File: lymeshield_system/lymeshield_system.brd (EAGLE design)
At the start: 67.9 x 49.5 mm, 67 parts, among them J1 TSW-106-07-G-S, J2 TSW-103-07-G-D-LL, J3 M04B, J4 1844210, U1 ATMEGA1608-MU, U10 MCP79410-I_SN, U12 STSPIN240, U2 MX25V1635FM1I, U3 STLQ015M33R, U4 DRV5057A2QDBZ, U5 OPA2349EA, Y1 ECS-.327-9-1210-TR, Y2 ECS-.327-9-1210-TR

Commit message: refactor: fixed ignored files and added tables
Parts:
- removed U10: MCP79410-I_SN, HatchPoint-MicrochipTechnology:SOIC127P600X175-8N
- removed U12: STSPIN240, HatchPoint-TI:VFQFPN(3X3X1.0MM-16L)
- added U6: DRV5057A2QDBZ, HatchPoint-TI:SOT95P237X112-3N
- added U7: STLQ015M33R, HatchPoint-ST:SOT23-5L
- C11: value 10nF -> 100nF
- C12: value 1000pF -> 22uF; device HatchPoint-Capacitors:CAPC_0603_1608X90N -> HatchPoint-Capacitors:CAPC_1206
- C13: value 10nF -> 2.2uF; device HatchPoint-Capacitors:CAPC_0603_1608X90N -> HatchPoint-Capacitors:CAPC_1206
- C14: value 22nF -> 10nF
- C15: value 1.00uF -> 10nF
- C16: value 1.00uF -> 100nF
- C17: value 22uF -> 1000pF; device HatchPoint-Capacitors:CAPC_1206 -> HatchPoint-Capacitors:CAPC_0603_1608X90N
- C18: value 2.2uF -> 22nF; device HatchPoint-Capacitors:CAPC_1206 -> HatchPoint-Capacitors:CAPC_0603_1608X90N
- C2: value 15.0pF -> 100nF; device HatchPoint-Capacitors:CAPC_0402_1005X55N -> HatchPoint-Capacitors:CAPC_0603_1608X90N
- C20, C21, C4: value 100nF -> 1.00uF
- C3: value 15.0pF -> 1.00uF; device HatchPoint-Capacitors:CAPC_0402_1005X55N -> HatchPoint-Capacitors:CAPC_0603_1608X90N
- C5, C6: value 1.00uF -> 15.0pF; device HatchPoint-Capacitors:CAPC_0603_1608X90N -> HatchPoint-Capacitors:CAPC_0402_1005X55N
- J2: value TSW-103-07-G-D-LL -> M04B; device HatchPoint-Samtec:HDRV6W64P254_2X3_762X495X838P -> HatchPoint-JST:SM04B-SRSS-TB(LFSN)
- J3: value M04B -> TSW-103-07-G-D-LL; device HatchPoint-JST:SM04B-SRSS-TB(LFSN) -> HatchPoint-Samtec:HDRV6W64P254_2X3_762X495X838P
- R1, R3: value 1.00K -> 4.70K
- R11: value 1.00K -> 620mOhm; device HatchPoint-Resistors:R0603K -> HatchPoint-Resistors:R0805K
- R12: value 47.0K -> 620mOhm; device HatchPoint-Resistors:R0603K -> HatchPoint-Resistors:R0805K
- R13: value 620mOhm -> 18.0K; device HatchPoint-Resistors:R0805K -> HatchPoint-Resistors:R0603K
- R14: value 620mOhm -> 1.00K; device HatchPoint-Resistors:R0805K -> HatchPoint-Resistors:R0603K
- R15: value 1.00K -> 47.0K
- R16, R17, R18: value 1.20M -> 1.00K
- R19, R20: value 1.00K -> 1.20M
- R4, R5: value 4.70K -> 1.00K
- R7, R8: value 18.0K -> 1.20M
- R9: value 1.20M -> 18.0K
- U1: value ATMEGA1608-MU -> MCP79410-I_SN; device HatchPoint-MicrochipTechnology:QFN50P500X500X90-33N -> HatchPoint-MicrochipTechnology:SOIC127P600X175-8N
- U2: value MX25V1635FM1I -> ATMEGA1608-MU; device HatchPoint-Macronix:SOIC127P600X175-8N -> HatchPoint-MicrochipTechnology:QFN50P500X500X90-33N
- U3: value STLQ015M33R -> MX25V1635FM1I; device HatchPoint-ST:SOT23-5L -> HatchPoint-Macronix:SOIC127P600X175-8N
- U4: value DRV5057A2QDBZ -> OPA2349EA; device HatchPoint-TI:SOT95P237X112-3N -> HatchPoint-OPAMPs:SOT65P280X145-8N
- U5: value OPA2349EA -> STSPIN240; device HatchPoint-OPAMPs:SOT65P280X145-8N -> HatchPoint-TI:VFQFPN(3X3X1.0MM-16L)
- moved R20 46.4 mm to (10.8, 12.1), turned to 180 degrees
- moved J2 46.3 mm to (19.1, 36.5), flipped to the top, turned to 180 degrees
- moved J3 46.3 mm to (60.6, 16.2), flipped to the bottom, turned to 270 degrees
- moved Q1 43.5 mm to (50.2, -5.08), turned to 0 degrees
- moved R1 42.1 mm to (21.6, 25.7), turned to 270 degrees
- moved R4 42.1 mm to (57.1, 3.17), turned to 0 degrees
- moved R5 41.6 mm to (57.1, 6.99), turned to 0 degrees
- moved Q3 41.1 mm to (11.7, 9.53), turned to 90 degrees
- moved C21 39.8 mm to (17.8, 11.1)
- moved R17 39.4 mm to (51.8, -9.84)
- moved R9 37.6 mm to (48.3, 15.7), turned to 270 degrees
- moved R16 36.6 mm to (47.3, -7.94)
- moved C16 34.3 mm to (47.3, -6.35), turned to 90 degrees
- moved C15 33.3 mm to (45.1, 14.3), turned to 90 degrees
- moved Q2 33.1 mm to (33.0, 34.9), turned to 270 degrees
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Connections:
- net !CS_FLASH: now also U3.1; no longer U1.1
- net !GRN_LED_EN: now also U2.11; no longer U1.11
- net !MTR_FAULT: now also J3.4, U2.15; no longer J2.4, U1.15
- net !MTR_STBY: now also C17.1, R13.2, U2.17, U5.14; no longer C12.1, R7.2, U1.17, U12.14
- net !RED_LED_EN: now also U2.10; no longer U1.10
- net !RST: now also C7.1, R3.2, U2.26; no longer C1.1, R2.2, U1.26
- net AN0_BAT_LVL: now also U2.13, U4.1, U4.2; no longer U1.13, U5.1, U5.2
- net AN1_HALL_FILT: now also U2.14, U4.6, U4.7; no longer U1.14, U5.6, U5.7
- net AVDD: now also C4.1, U2.18; no longer C6.1, U1.18
- net BKUP_BATTERY: now also Q2.1, U1.3; no longer Q1.1, U10.3
- net DGND: now also C11.1, C20.2, C21.2, J2.1, J2.5, Q1.2, Q2.3, R10.2, R11.2, R15.2, R19.2, R20.2, U1.4, U2.19, U2.29, U2.33, U3.4, U4.4, U5.17, U5.7, U7.2; no longer C11.2, C16.2, C20.1, J3.1, J3.5, Q1.3, Q3.2, R13.2, R14.2, R17.2, R18.2, R9.2, U1.19, U1.29, U1.33, U10.4, U12.17, U12.7, U2.4, U3.2, U5.4
- net GPIO_PC1: now also U2.7; no longer U1.7
- net HALL_PWM_SENSE: now also J3.5, R16.2, R17.1, U2.24, U6.2; no longer J2.5, R19.2, R20.1, U1.24, U4.2
- net HALL_PWR_EN: now also R18.1, U2.16; no longer R15.1, U1.16
- net I2C0_SCL: now also J2.4, R2.2, U1.6, U2.9; no longer J3.4, R5.2, U1.9, U10.6
- net I2C0_SDA: now also J2.3, R1.2, U1.5, U2.8; no longer J3.3, R4.2, U1.8, U10.5
- net MTR_CUR_LIMIT: now also J3.2, R9.1, U2.12; no longer J2.2, R6.1, U1.12
- net MTR_EN: now also R6.1, U2.22; no longer R10.1, U1.22
- net MTR_FAULT: now also C14.1, R6.2, U5.13; no longer C13.1, R10.2, U12.13
- net MTR_PHA: now also J3.1, U2.23, U5.1; no longer J2.1, U1.23, U12.1
- net MTR_PHB: now also U5.15; no longer U12.15
- net MTR_PWMA: now also J3.3, U2.25, U5.2; no longer J2.3, U1.25, U12.2
- net MTR_PWMB: now also U5.16; no longer U12.16
- net N$1: now also C8.1, U2.20, Y2.1; no longer C2.1, U1.20, Y1.1
- net N$10: now also R7.2, R8.1, U4.3; no longer R16.2, R17.1, U5.3
- net N$11: now also C18.1, R14.2; no longer C14.1, R11.2
- net N$14: now also Q3.2; no longer Q2.2
- net N$16: now also C9.1, U2.21, Y2.2; no longer C3.1, U1.21, Y1.2
- net N$17: now also C6.1, U1.1, Y1.2; no longer C9.1, U10.1, Y2.2
- net N$19: now also C15.1, R10.1, R9.2, U5.11; no longer C11.1, R6.2, R8.1, U12.11
- net N$2: now also C5.1, U1.2, Y1.1; no longer C8.1, U10.2, Y2.1
- net N$20: now also C19.1, R17.2, U4.5; no longer C21.1, R20.2, U5.5
- net N$23: now also C16.2, Q1.1, U6.3; no longer C21.2, Q3.1, U4.3
- net N$3: now also R14.1, R15.1, U5.12; no longer R11.1, R12.1, U12.12
- net N$5: now also Q1.3, R18.2, R19.1; no longer Q3.3, R15.2, R18.1
- net N$6: now also Q3.3, R20.1; no longer Q2.3, R9.1
- net N$7: now also Q2.2; no longer Q1.2
- net N$8: now also R4.2; no longer R1.2
- net N$9: now also R5.2; no longer R3.2
- net OUTA1: now also U5.3; no longer U12.3
- net OUTA2: now also U5.5; no longer U12.5
- net RTCC_ALARM_INT: now also U1.7, U2.32; no longer U1.32, U10.7
- net SENSEA: now also R11.1, R12.1, U5.4; no longer R13.1, R14.1, U12.4
- net SPI0_MISO: now also U2.3, U3.2; no longer U1.3, U2.2
- net SPI0_MOSI: now also U2.2, U3.5; no longer U1.2, U2.5
- net SPI0_SCK: now also U2.4, U3.6; no longer U1.4, U2.6
- net UART_RX: now also U2.31; no longer U1.31
- net UART_TX: now also U2.30; no longer U1.30
- net UPDI: now also U2.27; no longer U1.27
- net VCC: now also C1.1, C11.2, C2.1, C21.1, C3.1, J2.2, R13.1, R16.1, U1.8, U2.28, U3.8, U4.8, U6.1, U7.5; no longer C19.1, C20.2, C4.1, C5.1, C7.1, J3.2, R19.1, R7.1, U1.28, U10.8, U2.8, U3.5, U4.1, U5.8
- net V_BAT: now also C12.1, C13.1, C20.1, Q3.1, R7.1, U5.6, U7.1, U7.3; no longer C15.1, C17.1, C18.1, Q2.1, R16.1, U12.6, U3.1, U3.3

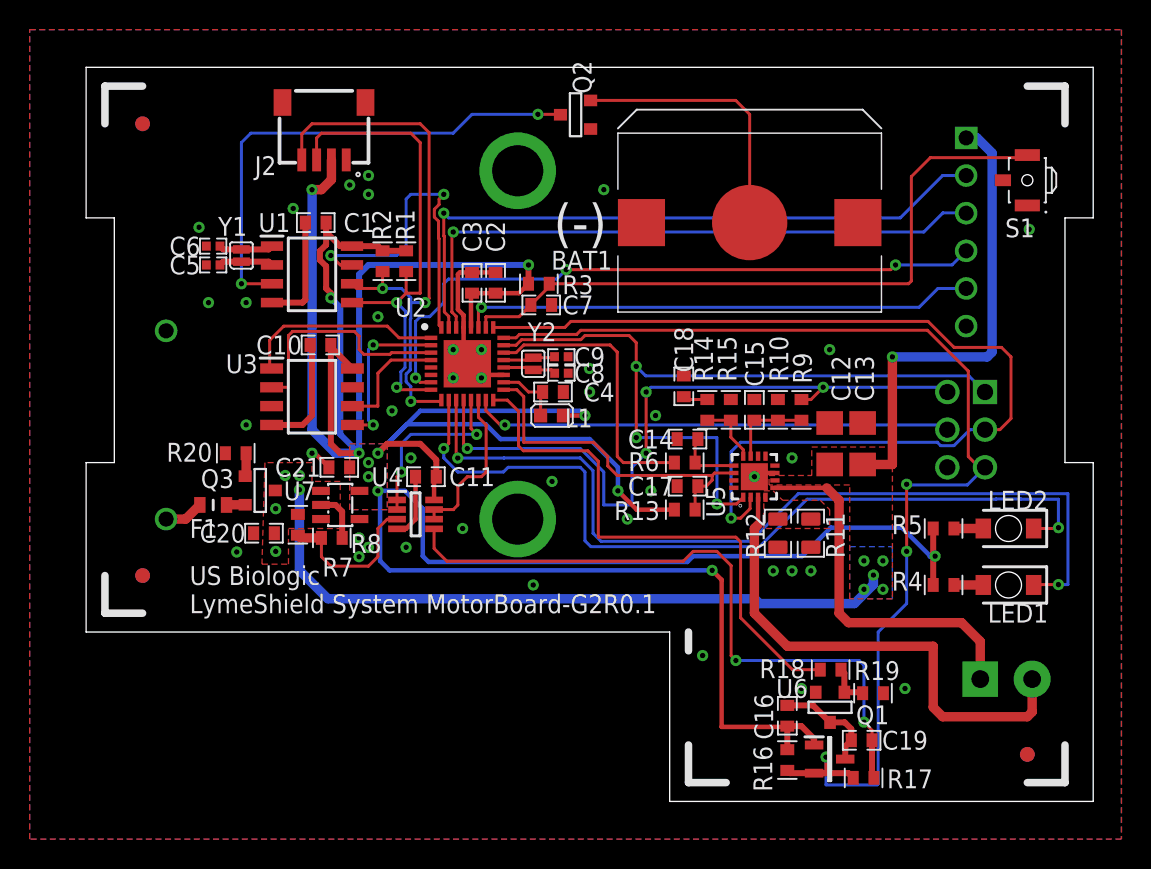
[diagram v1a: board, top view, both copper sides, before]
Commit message: feat: partial changes for r1,1 - Moved cur_limit to TBC0 pin - Modify layout to reduce EMI - Change programming header to match PICKit4 - Merge mtr_cur_limit into !mtr_cur_limit net
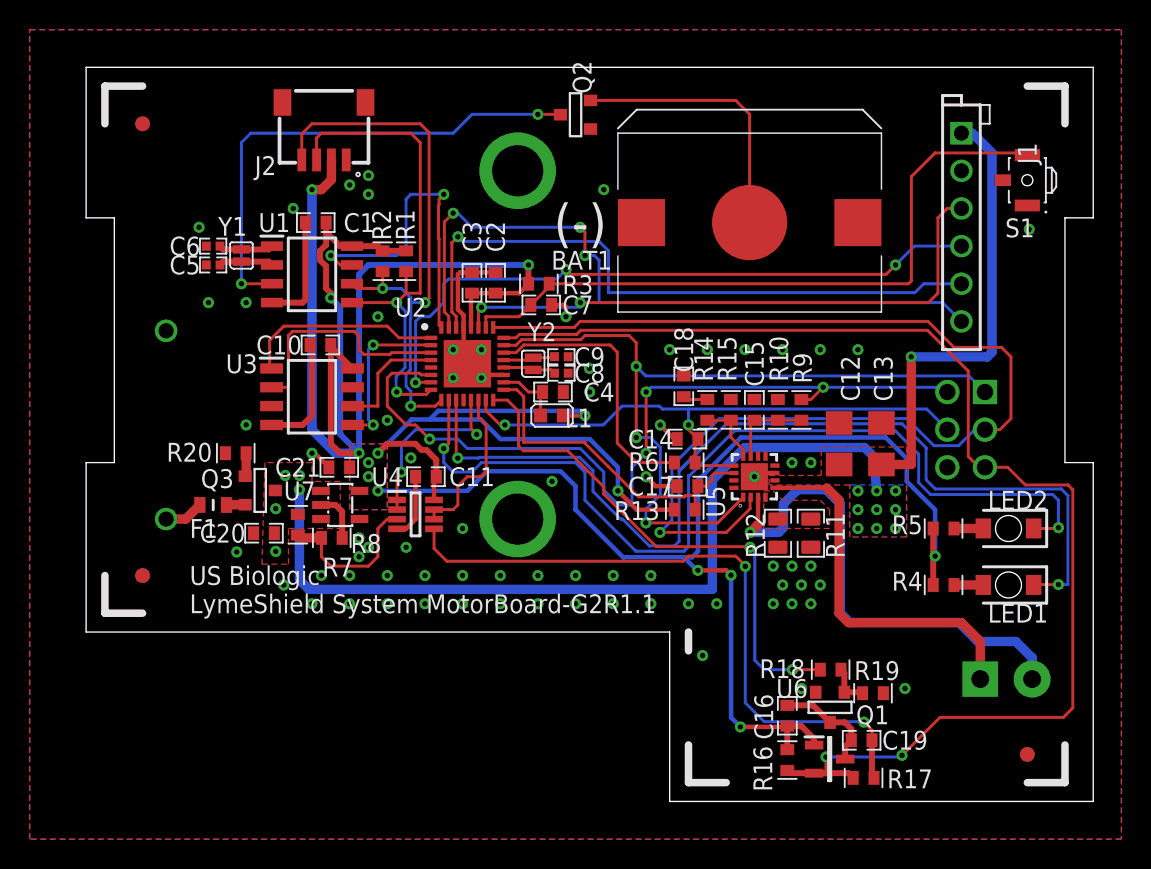
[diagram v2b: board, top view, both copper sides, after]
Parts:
- J1: value TSW-106-07-G-S -> TSW-106-16-L-S-RA; device HatchPoint-Samtec:HDR-100MIL-1X6-THRU -> HatchPoint-Samtec:HDR-100MIL-1X6-THRU-RA
- moved C13 1.27 mm to (53.7, 12.7)
- moved C12 0.63 mm to (50.8, 12.7)
- moved J1 0.45 mm to (59.1, 33.7), flipped to the top
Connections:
- removed net MTR_FAULT: C14.1, R6.2, U5.13
- net !MTR_FAULT: now also C14.1, R6.2, U5.13
- net DGND: now also J1.2; no longer J1.6
- net MTR_CUR_LIMIT: now also U2.6; no longer U2.12
- net UART_RX: now also J1.6; no longer J1.3
- net UART_TX: now also J1.5; no longer J1.2
- net UPDI: now also J1.3; no longer J1.5
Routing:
- net VCC: track 230.5 -> 211.6 mm, vias 12 -> 14
- net MTR_PWMA: track 67.1 -> 78.3 mm
- net V_BAT: track 78.0 -> 86.8 mm, vias 11 -> 15
- net !GRN_LED_EN: track 59.7 -> 68.5 mm
- net !MTR_FAULT: track 32.4 -> 40.1 mm, vias 1 -> 2
- net MTR_CUR_LIMIT: track 47.8 -> 55.4 mm
- net HALL_PWM_SENSE: track 78.7 -> 85.7 mm, vias 3 -> 2
- net !RED_LED_EN: track 55.9 -> 62.7 mm
- net DGND: track 36.6 -> 42.2 mm, vias 40 -> 74
- net UPDI: track 34.7 -> 39.8 mm, vias 1 -> 2
- net MTR_FAULT: track 4.36 -> 0.00 mm
- net UART_RX: track 44.4 -> 48.0 mm, vias 1 -> 3
- net MTR_PHA: track 52.0 -> 54.8 mm
- net UART_TX: track 41.7 -> 43.8 mm
- net HALL_PWR_EN: track 37.0 -> 35.6 mm, vias 0 -> 2
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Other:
- board text added: "US Biologic LymeShield System MotorBoard-G2R1.1"
- board text added: "VCC GND PDG GPIO TXD RXD"
- board text removed: "US Biologic LymeShield System MotorBoard-G2R0.1"
- board text removed: "VCC TXD RXD GPIO OPDI GND"

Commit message: fix: updates for R2.1 board - Change layout for high current routes - Correct routing errors (mtr_cur_limit) - Change tantalum cap to 1210 and give more space
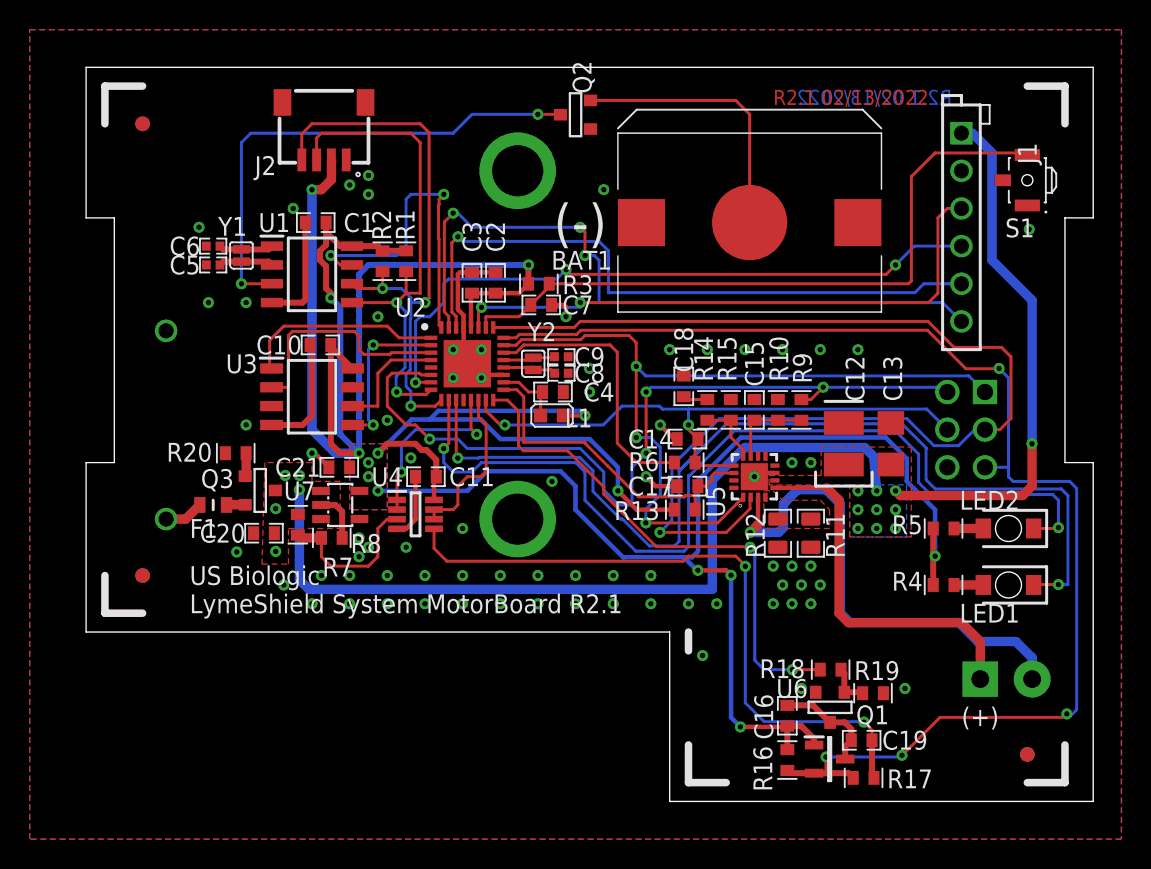
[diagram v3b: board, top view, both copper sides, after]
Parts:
- C12: value 22uF -> TAJB226M010RNJ; device HatchPoint-Capacitors:CAPC_1206 -> HatchPoint-Capacitors:PCAPC_1210
- moved C13 0.63 mm to (54.3, 12.7)
- moved C12 0.32 mm to (51.1, 12.7)
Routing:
- net V_BAT: track 86.8 -> 91.8 mm
- net HALL_PWM_SENSE: track 85.7 -> 88.7 mm, vias 2 -> 4
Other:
- board text added: "(+)"
- board text added: "R2.1 02/13/2022"
- board text added: "US Biologic LymeShield System MotorBoard R2.1"
- board text removed: "US Biologic LymeShield System MotorBoard Gen2 R0.1"
- board text removed: "US Biologic LymeShield System MotorBoard-G2R1.1"

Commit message: fix(lss):  update to R2.2 - Change motor driver
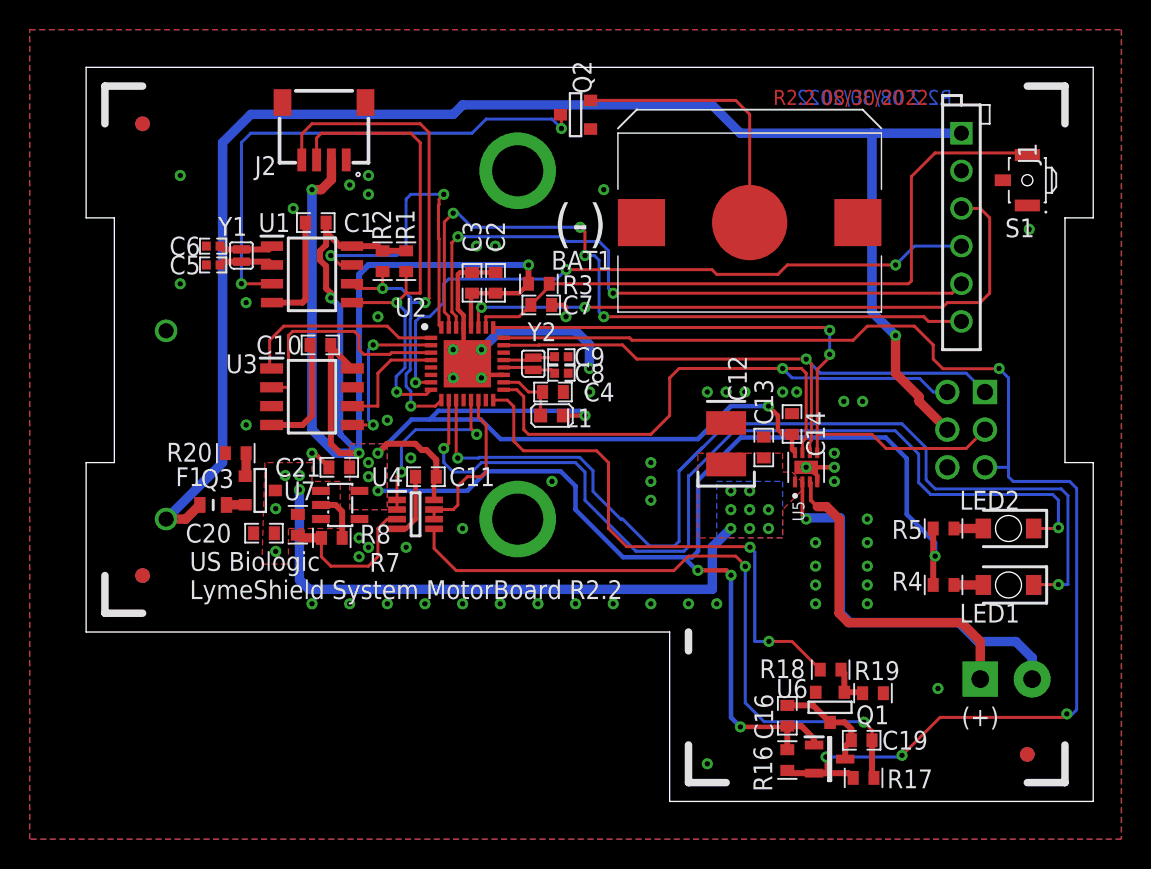
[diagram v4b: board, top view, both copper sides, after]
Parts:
- removed C15: 10nF, HatchPoint-Capacitors:CAPC_0603_1608X90N
- removed C17: 1000pF, HatchPoint-Capacitors:CAPC_0603_1608X90N
- removed C18: 22nF, HatchPoint-Capacitors:CAPC_0603_1608X90N
- removed R10, R13, R6, R9: 18.0K, HatchPoint-Resistors:R0603K
- removed R11, R12: 620mOhm, HatchPoint-Resistors:R0805K
- removed R14: 1.00K, HatchPoint-Resistors:R0603K
- removed R15: 47.0K, HatchPoint-Resistors:R0603K
- C13: value 2.2uF -> 100nF; device HatchPoint-Capacitors:CAPC_1206 -> HatchPoint-Capacitors:CAPC_0603_1608X90N
- C14: value 10nF -> 100nF
- U5: value STSPIN240 -> DRV8838DSGR; device HatchPoint-TI:VFQFPN(3X3X1.0MM-16L) -> HatchPoint-MotionControl:SON50P200X200X80-9N
- moved C13 8.63 mm to (45.7, 11.7)
- moved C12 7.94 mm to (43.2, 12.7)
- moved C14 6.36 mm to (47.6, 13.3), turned to 90 degrees
- moved U5 3.55 mm to (48.6, 11.1)
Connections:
- removed net !MTR_FAULT: C14.1, J3.4, R6.2, U2.15, U5.13
- removed net MTR_CUR_LIMIT: J3.2, R9.1, U2.6
- removed net MTR_EN: R6.1, U2.22
- removed net MTR_PHB: U5.15
- removed net MTR_PWMB: U5.16
- removed net N$11: C18.1, R14.2
- removed net N$15: BAT2.1, F1.1
- removed net N$19: C15.1, R10.1, R9.2, U5.11
- removed net N$3: R14.1, R15.1, U5.12
- removed net SENSEA: R11.1, R12.1, U5.4
- new net V_BAT_IN: BAT2.1, F1.1, J1.1, J3.4
- net !MTR_STBY: now also J3.2, U5.7; no longer C17.1, R13.2, U5.14
- net DGND: now also U5.4, U5.9; no longer C15.2, C17.2, C18.2, R10.2, R11.2, R12.2, R15.2, U5.17, U5.7
- net MTR_PHA: now also U5.6; no longer U5.1
- net MTR_PWMA: now also U5.5; no longer U5.2
- net OUTA1: now also U5.2; no longer U5.3
- net OUTA2: now also U5.3; no longer U5.5
- net VCC: now also C14.1, U5.8; no longer R13.1
- net V_BAT: now also U5.1; no longer J1.1, U5.6
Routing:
- net V_BAT_IN: track 0.00 -> 103.4 mm, vias 0 -> 1
- net MTR_CUR_LIMIT: track 55.4 -> 0.00 mm, vias 4 -> 0
- net V_BAT: track 91.8 -> 38.8 mm, vias 15 -> 13
- net !MTR_FAULT: track 40.1 -> 0.00 mm, vias 2 -> 0
- net MTR_PWMA: track 78.3 -> 43.6 mm, vias 1 -> 2
- net !MTR_STBY: track 22.4 -> 43.7 mm, vias 0 -> 1
- net MTR_EN: track 18.6 -> 0.00 mm
- net MTR_PHA: track 54.8 -> 40.3 mm, vias 3 -> 1
- net DGND: track 42.2 -> 52.6 mm, vias 74 -> 66
- net VCC: track 211.6 -> 220.2 mm
- net OUTA1: track 34.2 -> 27.0 mm
- net N$19: track 5.70 -> 0.00 mm
- net N$3: track 4.36 -> 0.00 mm
- net UPDI: track 39.8 -> 43.4 mm
- net N$15: track 2.67 -> 0.00 mm
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- removed copper zone on layer 1, net SENSEA
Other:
- board text added: "!STBY VBAT GND"
- board text added: "R2.2 08/30/2022"
- board text added: "US Biologic LymeShield System MotorBoard R2.2"
- board text removed: "LIMIT FAULT GND"
- board text removed: "R2.1 02/13/2022"
- board text removed: "US Biologic LymeShield System MotorBoard R2.1"
